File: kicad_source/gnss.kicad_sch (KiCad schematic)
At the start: 10 parts, among them U3 MAX-M10S

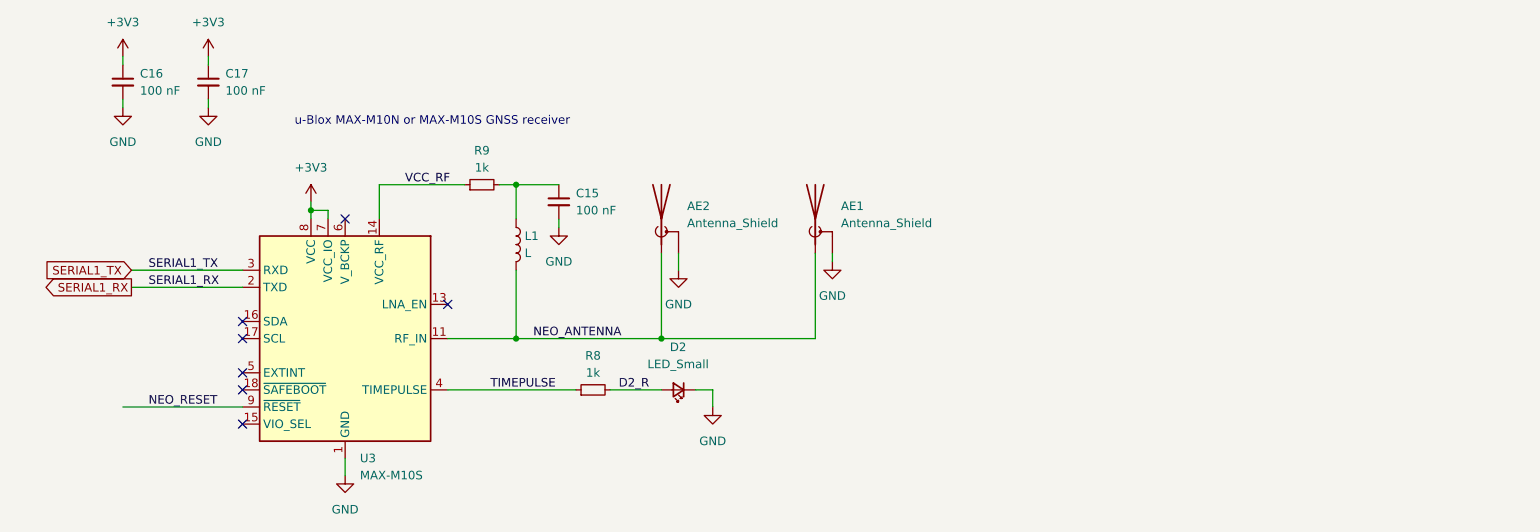
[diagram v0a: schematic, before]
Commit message: added battery holder for GNSS backup
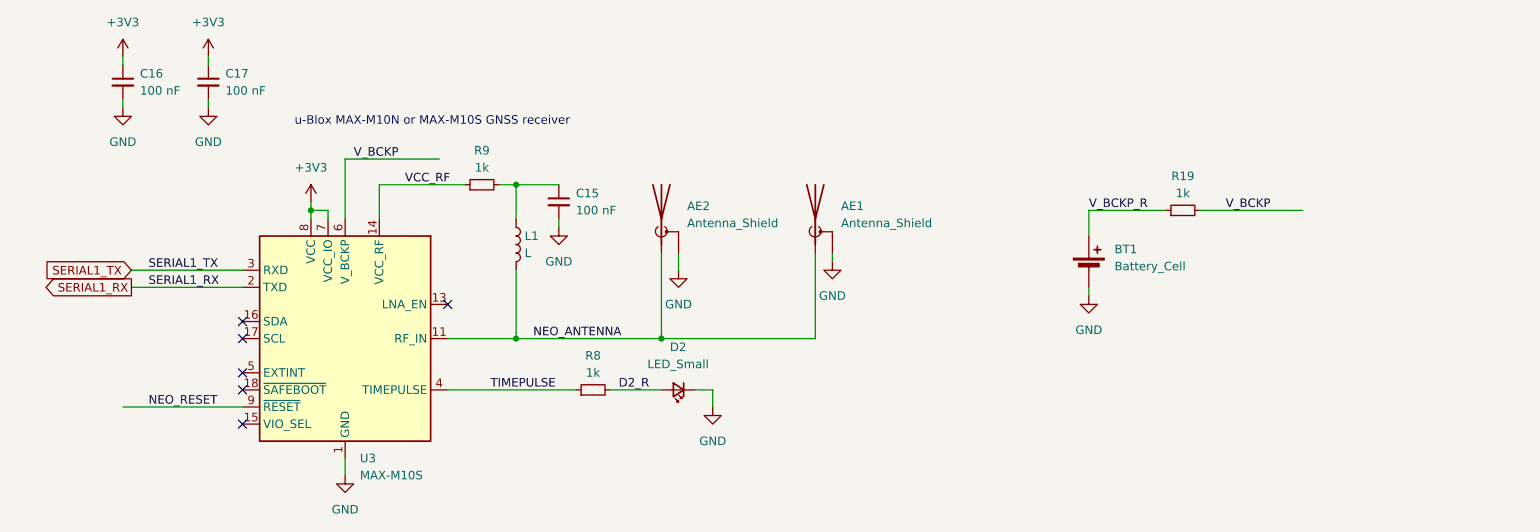
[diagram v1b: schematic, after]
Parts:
- added BT1: Battery_Cell, Battery:BatteryHolder_Keystone_3000_1x12mm, symbol Device:Battery_Cell
- added R19: 1k, Resistor_SMD:R_0603_1608Metric, symbol Device:R_Small
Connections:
- net GND: now also BT1.2 (-)
- net V_BCKP: now reaches U3.6 (V_BCKP)
- net V_BCKP: now also R19.2
- new net V_BCKP_R: BT1.1 (+), R19.1
- no-connect marks 7 -> 6

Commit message: connected reset of BNO055 and GNSS module, updated layout
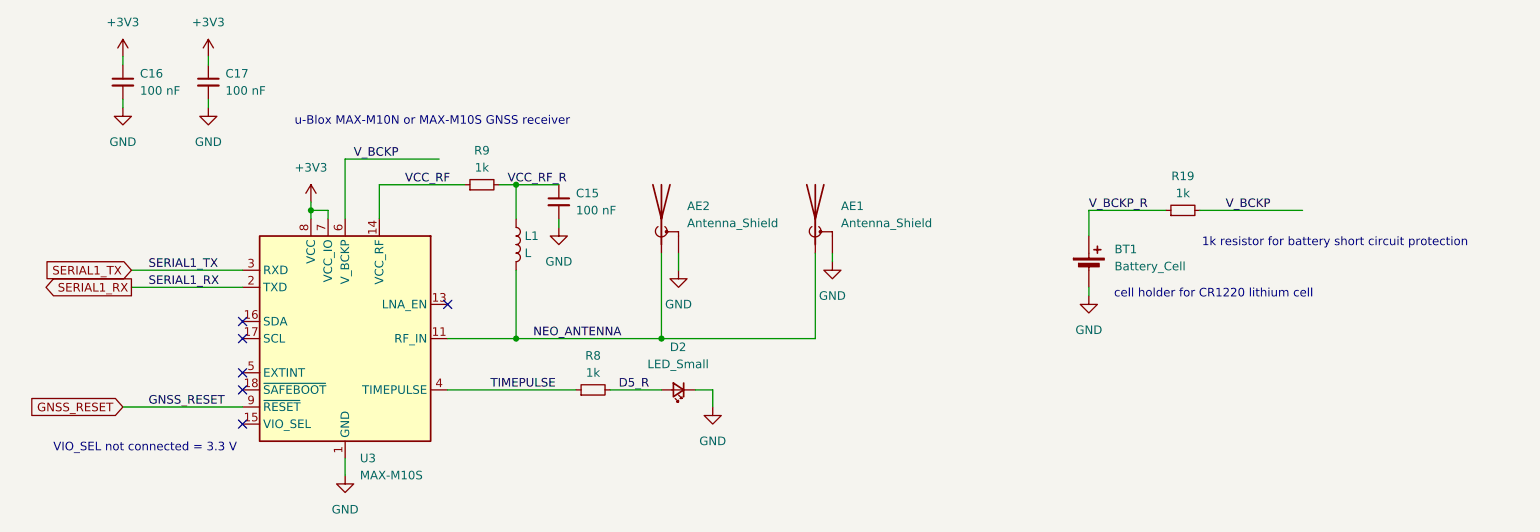
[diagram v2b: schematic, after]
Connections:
- net VCC_RF_R: now reaches C15.1, L1.1, R9.2
- net D2_R renamed D5_R
- net NEO_RESET renamed GNSS_RESET
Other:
- note added: "1k resistor for battery short circuit protection"
- note added: "VIO_SEL not connected = 3.3 V"
- note added: "cell holder for CR1220 lithium cell"
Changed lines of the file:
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@@
+		)
+	)
+	(text "cell holder for CR1220 lithium cell"
+		(exclude_from_sim no)
+		(at 216.662 61.976 0)
+		(effects
+			(font
+				(size 1.27 1.27)
+			)
+		)
+	)
+	(text "1k resistor for battery short circuit protection"
+		(exclude_from_sim no)
+		(at 234.696 54.356 0)
+		(effects
+			(font
+				(size 1.27 1.27)
+			)
+		)
+	)
+	(text "VIO_SEL not connected = 3.3 V"
+		(exclude_from_sim no)
+		(at 57.912 84.836 0)
+		(effects
+			(font
+				(size 1.27 1.27)
+			)
 		)
 	)
@@
 		)
 	)
-	(label "D2_R"
+	(label "VCC_RF_R"
+		(at 111.76 45.72 0)
+		(effects
+			(font
+				(size 1.27 1.27)
+			)
+			(justify left bottom)
+		)
+	)
+	(label "D5_R"
 		(at 128.27 76.2 0)
 		(effects
@@
 		)
 	)
-	(label "NEO_RESET"
+	(label "GNSS_RESET"
 		(at 58.42 78.74 0)
 		(effects
@@
 			(effects
 				(font
+					(size 1.27 1.27)
+				)
+				(justify right)
+				(hide yes)
+			)
+		)
+	)
+	(global_label "GNSS_RESET"
+		(shape input)
+		(at 54.61 78.74 180)
+		(fields_autoplaced yes)
+		(effects
+			(font
+				(size 1.27 1.27)
+			)
+			(justify right)
+		)
+		(property "Intersheetrefs" "${INTERSHEET_REFS}"
+			(at 40.5468 78.74 0)
+			(effects
+				(font
